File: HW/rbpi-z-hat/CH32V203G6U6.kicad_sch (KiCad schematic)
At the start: 19 parts, among them J11 Conn_01x10, J12 Conn_01x06, J13 Conn_01x10, J14 Conn_01x06, J15 Conn_01x06, J16 Conn_01x10, U7 STM32F031G6Ux, X2 ASEMB-25.000MHZ-LC-T

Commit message: Some update...
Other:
- note added: "OT322525MJBA4SL"
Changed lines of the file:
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@@
     (stroke (width 0) (type default))
+  )
+  (text "OT322525MJBA4SL" (at 74.93 171.45 0)
+    (effects (font (size 1.27 1.27)) (justify left bottom))
   )
   (text "CH32V203G6U6" (at 111.76 114.3 90)

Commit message: Changes in Sch & PCB
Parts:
- C20, C21: footprint Capacitor_SMD:C_0805_2012Metric -> Capacitor_SMD:C_0603_1608Metric
- C32, C33, C34: footprint Capacitor_SMD:C_0603_1608Metric -> Capacitor_SMD:C_0402_1005Metric
- L10: footprint Inductor_SMD:L_0805_2012Metric -> Inductor_SMD:L_0603_1608Metric
- R12: footprint Resistor_SMD:R_0603_1608Metric -> Resistor_SMD:R_0402_1005Metric
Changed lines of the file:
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@@
       (effects (font (size 1.27 1.27)) (justify left))
     )
-    (property "Footprint" "Capacitor_SMD:C_0805_2012Metric" (at 54.3052 220.98 0)
+    (property "Footprint" "Capacitor_SMD:C_0603_1608Metric" (at 54.3052 220.98 0)
       (effects (font (size 1.27 1.27)) hide)
     )
@@
       (effects (font (size 1.27 1.27)) (justify left))
     )
-    (property "Footprint" "Capacitor_SMD:C_0805_2012Metric" (at 36.5252 220.98 0)
+    (property "Footprint" "Capacitor_SMD:C_0603_1608Metric" (at 36.5252 220.98 0)
       (effects (font (size 1.27 1.27)) hide)
     )
@@
       (effects (font (size 1.27 1.27)) (justify left))
     )
-    (property "Footprint" "Capacitor_SMD:C_0603_1608Metric" (at 63.8048 220.98 0)
+    (property "Footprint" "Capacitor_SMD:C_0402_1005Metric" (at 63.8048 220.98 0)
       (effects (font (size 1.27 1.27)) hide)
     )
@@
       (effects (font (size 1.27 1.27)) (justify left))
     )
-    (property "Footprint" "Capacitor_SMD:C_0603_1608Metric" (at 71.4248 220.98 0)
+    (property "Footprint" "Capacitor_SMD:C_0402_1005Metric" (at 71.4248 220.98 0)
       (effects (font (size 1.27 1.27)) hide)
     )
@@
       (effects (font (size 1.27 1.27)))
     )
-    (property "Footprint" "Resistor_SMD:R_0603_1608Metric" (at 72.39 103.378 90)
+    (property "Footprint" "Resistor_SMD:R_0402_1005Metric" (at 72.39 103.378 90)
       (effects (font (size 1.27 1.27)) hide)
     )
@@
       (effects (font (size 1.27 1.27)))
     )
-    (property "Footprint" "Inductor_SMD:L_0805_2012Metric" (at 44.45 210.058 90)
+    (property "Footprint" "Inductor_SMD:L_0603_1608Metric" (at 44.45 210.058 90)
       (effects (font (size 1.27 1.27)) hide)
     )
@@
       (effects (font (size 1.27 1.27)) (justify left))
     )
-    (property "Footprint" "Capacitor_SMD:C_0603_1608Metric" (at 56.1848 166.37 0)
-      (effects (font (size 1.27 1.27)) hide)
-    )
+    (property "Footprint" "Capacitor_SMD:C_0402_1005Metric" (at 56.1848 166.37 0)
+      (effects (font (size 1.27 1.27)) hide)
+    )

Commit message: Updated CH32V203G6U6.kicad_sch
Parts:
- added C23: 0.1uF, Capacitor_SMD:C_0402_1005Metric, symbol Device:C
- added R4: 10K, Resistor_SMD:R_0402_1005Metric, symbol Device:R
- added R5: 500K, Resistor_SMD:R_0402_1005Metric, symbol Device:R
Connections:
- net CH32_SCK: now also U7.27 (PB6); no longer U7.9 (PA3)
- net CH32_SDA: now also U7.28 (PB7); no longer U7.10 (PA4)
- net CH32_VDD: now also R4.2
- net GNDD: now also C23.2, R5.1
- net PWM_OUT5: now also U7.9 (PA3); no longer U7.27 (PB6)
- net PWM_OUT6: now also U7.10 (PA4); no longer U7.28 (PB7)
- net at U7.1 (BOOT0): now also R5.2
- net CH32_nRST: now reaches U7.4 (NRST)
- net CH32_nRST: now also C23.1, R4.1

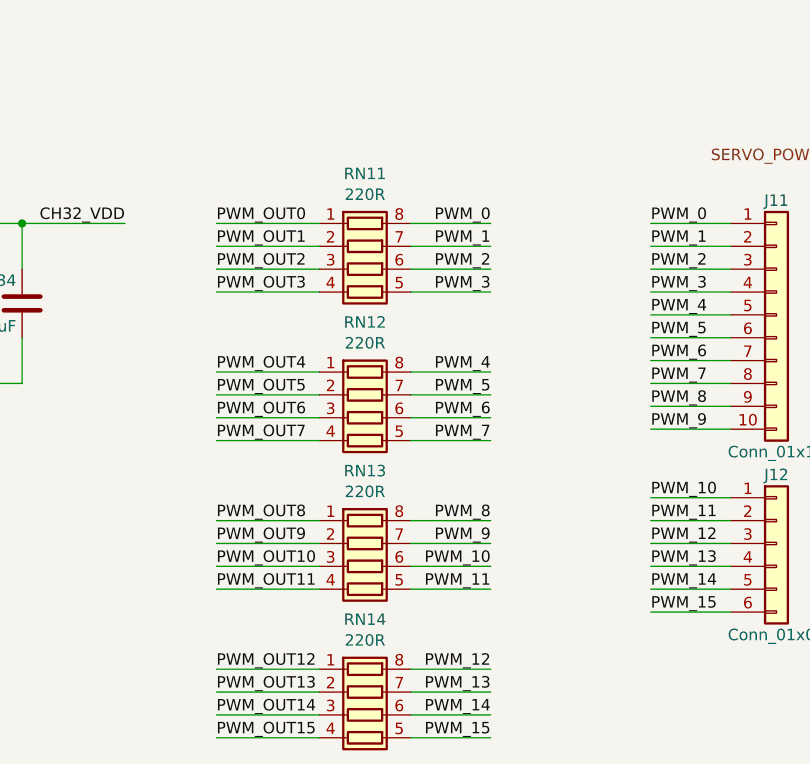
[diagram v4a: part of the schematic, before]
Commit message: Changed some footprints
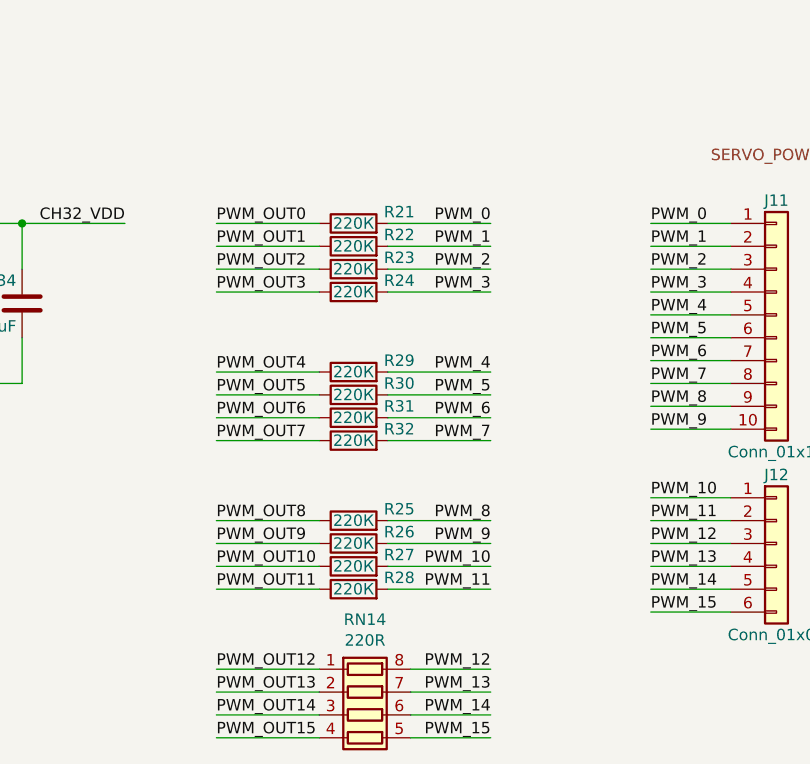
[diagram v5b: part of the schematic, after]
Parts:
- removed RN11, RN12, RN13: 220R, Resistor_SMD:R_Array_Concave_4x0603, symbol Device:R_Pack04
- added R21, R22, R23, R24, R25, R26, R27, R28, R29, R30, R31, R32: 220К, Resistor_SMD:R_0402_1005Metric, symbol Device:R
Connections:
- net PWM_0: now also R21.2
- net PWM_1: now also R22.2
- net PWM_10: now also R27.2
- net PWM_11: now also R28.2
- net PWM_2: now also R23.2
- net PWM_3: now also R24.2
- net PWM_4: now also R29.2
- net PWM_5: now also R30.2
- net PWM_6: now also R31.2
- net PWM_7: now also R32.2
- net PWM_8: now also R25.2
- net PWM_9: now also R26.2
- net PWM_OUT0: now also R21.1
- net PWM_OUT1: now also R22.1
- net PWM_OUT10: now also R27.1
- net PWM_OUT11: now also R28.1
- net PWM_OUT2: now also R23.1
- net PWM_OUT3: now also R24.1
- net PWM_OUT4: now also R29.1
- net PWM_OUT5: now also R30.1
- net PWM_OUT6: now also R31.1
- net PWM_OUT7: now also R32.1
- net PWM_OUT8: now also R25.1
- net PWM_OUT9: now also R26.1

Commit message: Changed some footprints
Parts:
- removed RN14: 220R, Resistor_SMD:R_Array_Concave_4x0603, symbol Device:R_Pack04
- added R37, R38, R39, R40: 220К, Resistor_SMD:R_0402_1005Metric, symbol Device:R
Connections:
- net PWM_12: now also R37.2
- net PWM_13: now also R38.2
- net PWM_14: now also R39.2
- net PWM_15: now also R40.2
- net PWM_OUT12: now also R37.1
- net PWM_OUT13: now also R38.1
- net PWM_OUT14: now also R39.1
- net PWM_OUT15: now also R40.1
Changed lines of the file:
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@@
     (stroke (width 0) (type default))
   )
-  (wire (pts (xy 115.57 265.43) (xy 124.46 265.43))
+  (wire (pts (xy 113.03 265.43) (xy 124.46 265.43))
     (stroke (width 0) (type default))
   )
@@
     (stroke (width 0) (type default))
   )
-  (wire (pts (xy 115.57 257.81) (xy 124.46 257.81))
+  (wire (pts (xy 113.03 257.81) (xy 124.46 257.81))
     (stroke (width 0) (type default))
   )
@@
     (stroke (width 0) (type default))
   )
-  (wire (pts (xy 115.57 262.89) (xy 124.46 262.89))
+  (wire (pts (xy 113.03 262.89) (xy 124.46 262.89))
     (stroke (width 0) (type default))
   )
@@
     (stroke (width 0) (type default))
   )
-  (wire (pts (xy 115.57 260.35) (xy 124.46 260.35))
+  (wire (pts (xy 113.03 260.35) (xy 124.46 260.35))
     (stroke (width 0) (type default))
   )
@@
         (path "/d99b0340-d795-4b40-9cde-9851c6cee99d/6f858a9a-df12-47bc-8e08-dc24a46c0b66"
           (reference "C21") (unit 1)
-        )
-      )
-    )
-  )
-  (symbol (lib_id "Device:R_Pack04") (at 110.49 262.89 270) (unit 1)
-    (in_bom yes) (on_board yes) (dnp no)
-    (property "Reference" "RN14" (at 110.49 252.2982 90)
-      (effects (font (size 1.27 1.27)))
-    )
-    (property "Value" "220R" (at 110.49 254.6096 90)
-      (effects (font (size 1.27 1.27)))
-    )
-    (property "Footprint" "Resistor_SMD:R_Array_Concave_4x0603" (at 110.49 269.875 90)
-      (effects (font (size 1.27 1.27)) hide)
-    )
-    (property "Datasheet" "~" (at 110.49 262.89 0)
-      (effects (font (size 1.27 1.27)) hide)
-    )
-    (pin "1")
-    (pin "2")
-    (pin "3")
-    (pin "4")
-    (pin "5")
-    (pin "6")
-    (pin "7")
-    (pin "8")
-    (instances
-      (project "rbpi-z-hat"
-        (path "/d99b0340-d795-4b40-9cde-9851c6cee99d/6f858a9a-df12-47bc-8e08-dc24a46c0b66"
-          (reference "RN14") (unit 1)
         )
       )
@@
     )
   )
+  (symbol (lib_id "Device:R") (at 109.22 257.81 90) (unit 1)
+    (in_bom yes) (on_board yes) (dnp no)
+    (property "Reference" "R37" (at 114.3 256.54 90)
+      (effects (font (size 1.27 1.27)))
+    )
+    (property "Value" "220К" (at 109.22 257.81 90)
+      (effects (font (size 1.27 1.27)))
+    )
+    (property "Footprint" "Resistor_SMD:R_0402_1005Metric" (at 109.22 259.588 90)
+      (effects (font (size 1.27 1.27)) hide)
+    )
+    (property "Datasheet" "~" (at 109.22 257.81 0)
+      (effects (font (size 1.27 1.27)) hide)
+    )
+    (pin "1")
+    (pin "2")
+    (instances
+      (project "rbpi-z-hat"
+        (path "/d99b0340-d795-4b40-9cde-9851c6cee99d/6f858a9a-df12-47bc-8e08-dc24a46c0b66"
+          (reference "R37") (unit 1)
+        )
+      )
+    )
+  )
   (symbol (lib_id "Device:R") (at 109.22 232.41 90) (unit 1)
     (in_bom yes) (on_board yes) (dnp no)
@@
         )
       )
+    )
+  )
+  (symbol (lib_id "Device:R") (at 109.22 260.35 90) (unit 1)
+    (in_bom yes) (on_board yes) (dnp no)
+    (property "Reference" "R38" (at 114.3 259.08 90)
+      (effects (font (size 1.27 1.27)))
+    )
+    (property "Value" "220К" (at 109.22 260.35 90)
+      (effects (font (size 1.27 1.27)))
+    )
+    (property "Footprint" "Resistor_SMD:R_0402_1005Metric" (at 109.22 262.128 90)
+      (effects (font (size 1.27 1.27)) hide)
+    )
+    (property "Datasheet" "~" (at 109.22 260.35 0)
+      (effects (font (size 1.27 1.27)) hide)
+    )
+    (pin "1")
+    (pin "2")
+    (instances
+      (project "rbpi-z-hat"
+        (path "/d99b0340-d795-4b40-9cde-9851c6cee99d/6f858a9a-df12-47bc-8e08-dc24a46c0b66"
+          (reference "R38") (unit 1)
+        )
+      )
+    )
+  )
+  (symbol (lib_id "Device:R") (at 109.22 262.89 90) (unit 1)
+    (in_bom yes) (on_board yes) (dnp no)
+    (property "Reference" "R39" (at 114.3 261.62 90)
+      (effects (font (size 1.27 1.27)))
+    )
+    (property "Value" "220К" (at 109.22 262.89 90)
+      (effects (font (size 1.27 1.27)))
+    )
+    (property "Footprint" "Resistor_SMD:R_0402_1005Metric" (at 109.22 264.668 90)
+      (effects (font (size 1.27 1.27)) hide)
+    )
+    (property "Datasheet" "~" (at 109.22 262.89 0)
+      (effects (font (size 1.27 1.27)) hide)
+    )
+    (pin "1")
+    (pin "2")
+    (instances
+      (project "rbpi-z-hat"
+        (path "/d99b0340-d795-4b40-9cde-9851c6cee99d/6f858a9a-df12-47bc-8e08-dc24a46c0b66"
+          (reference "R39") (unit 1)
+        )
+      )
+    )
+  )
+  (symbol (lib_id "Device:R") (at 109.22 265.43 90) (unit 1)
+    (in_bom yes) (on_board yes) (dnp no)
+    (property "Reference" "R40" (at 114.3 264.16 90)
+      (effects (font (size 1.27 1.27)))
+    )
+    (property "Value" "220К" (at 109.22 265.43 90)
+      (effects (font (size 1.27 1.27)))
+    )
+    (property "Footprint" "Resistor_SMD:R_0402_1005Metric" (at 109.22 267.208 90)
+      (effects (font (size 1.27 1.27)) hide)
+    )
+    (property "Datasheet" "~" (at 109.22 265.43 0)
+      (effects (font (size 1.27 1.27)) hide)
+    )
+    (pin "1")
+    (pin "2")
+    (instances
+      (project "rbpi-z-hat"
+        (path "/d99b0340-d795-4b40-9cde-9851c6cee99d/6f858a9a-df12-47bc-8e08-dc24a46c0b66"
+          (reference "R40") (unit 1)
+        )
+      )
